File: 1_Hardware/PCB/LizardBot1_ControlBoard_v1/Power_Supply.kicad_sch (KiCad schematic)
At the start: 48 parts, among them J201 XT60-M, J202 Receptable-5.08-2P, J203 JST-PH-2-Male, J204 JST-PH-2-Male, J205 JST-PH-2-Male, J206 USB_C_Receptacle_PowerOnly_6P, Q201 SQ4425EY, SW201 SW_SPST, SW202 SW_Push, SW203 SW_SPDT, U201 MP2225, U202 AP2112K-3.3

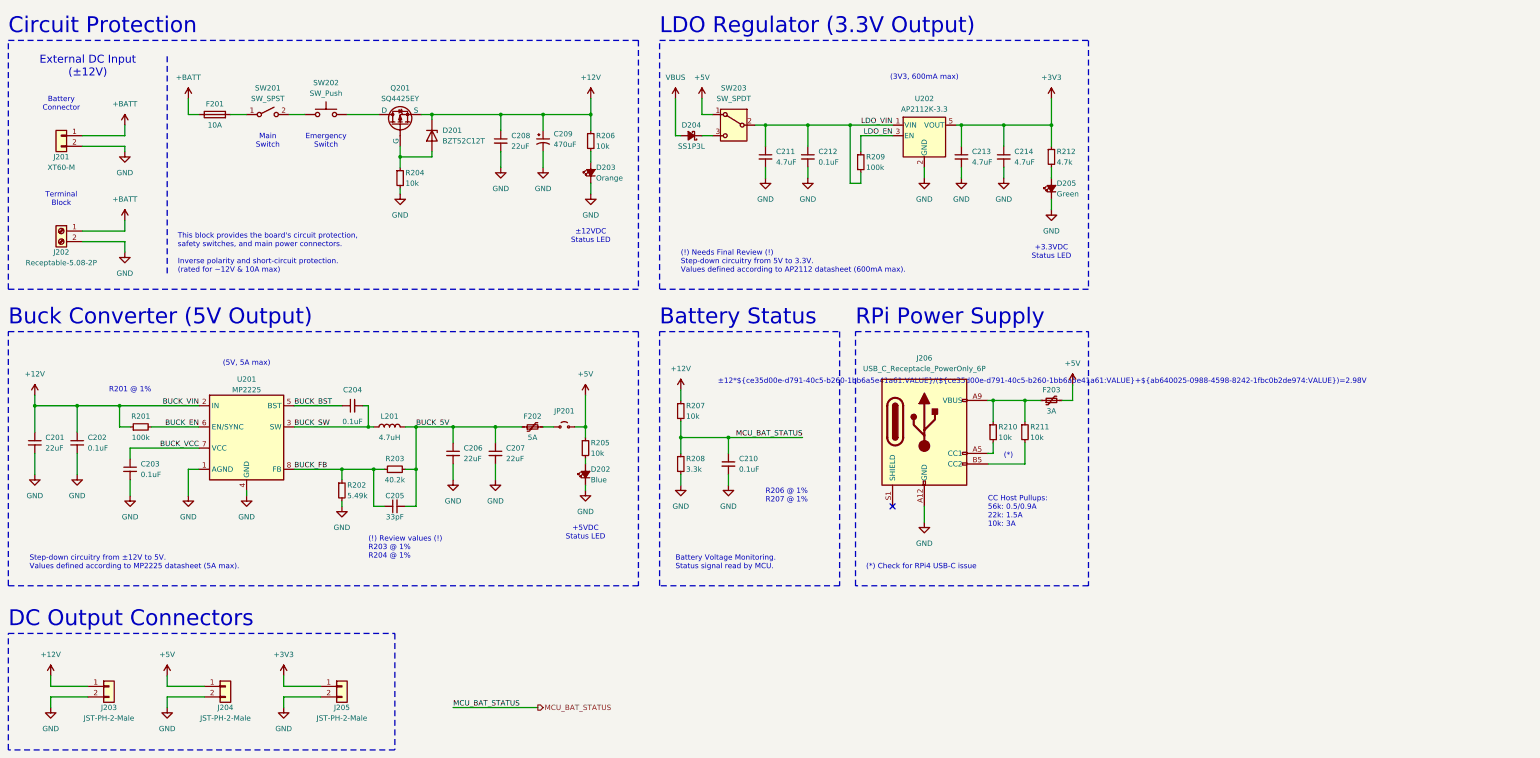
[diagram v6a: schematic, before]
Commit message: Updated schematics. Assigned footprints. Added BOM to /4_Docs.
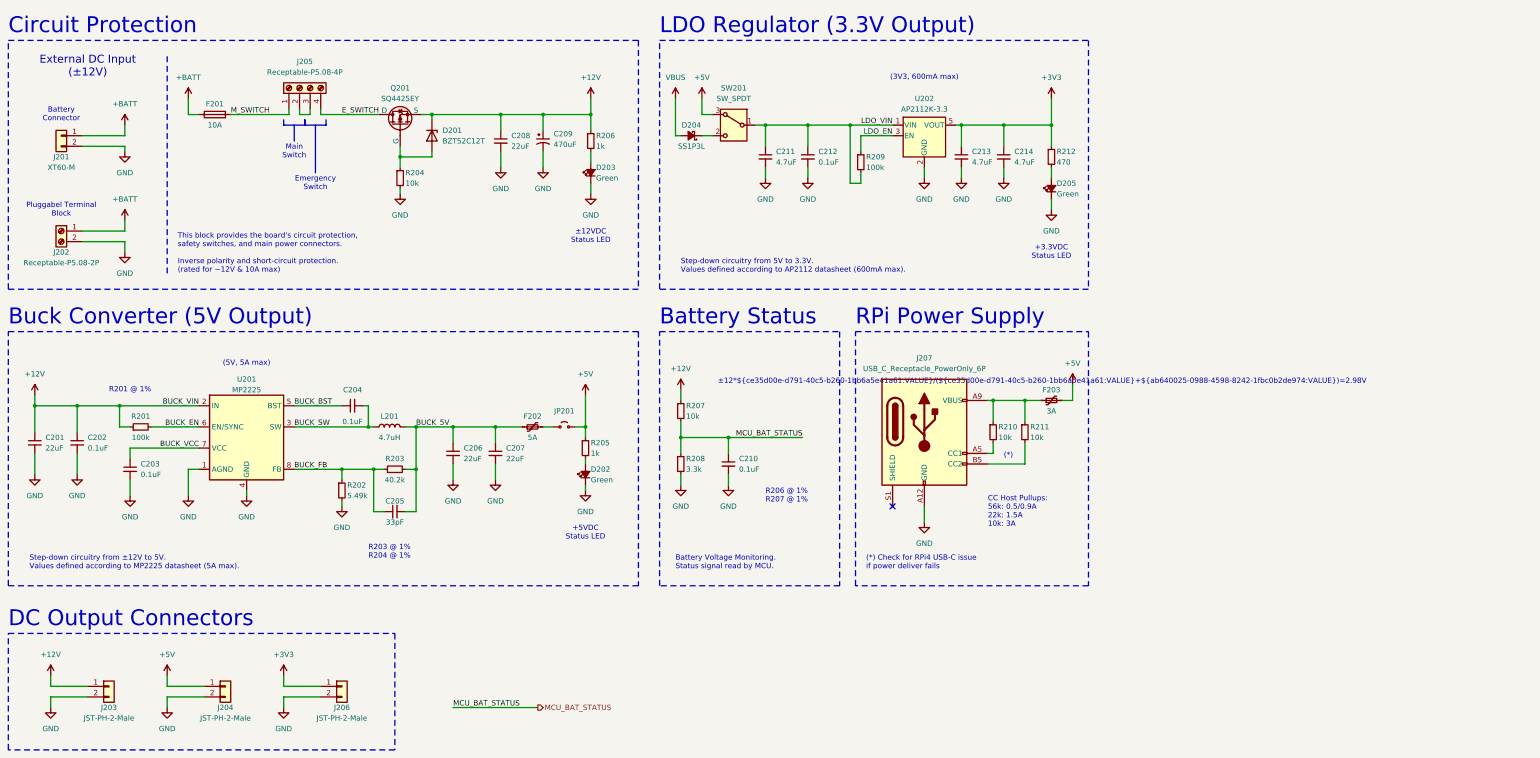
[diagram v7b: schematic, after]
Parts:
- removed SW201: SW_SPST, symbol Switch:SW_SPST
- removed SW202: SW_Push, symbol Switch:SW_Push
- removed SW203: SW_SPDT, symbol Switch:SW_SPDT
- added J205: Receptable-P5.08-4P, Connector_Phoenix_MSTB:PhoenixContact_MSTBA_2,5_4-G-5,08_1x04_P5.08mm_Horizontal, symbol Connector:Screw_Terminal_01x04
- added SW201: SW_SPDT, Button_Switch_THT:SW_Slide_SPDT_Straight_CK_OS102011MS2Q, symbol Switch:SW_SPDT_312
- C201, C202, C206, C207, C208, C211, C212, C213, C214: footprint (none) -> Capacitor_SMD:C_0805_2012Metric_Pad1.18x1.45mm_HandSolder
- C203, C204, C205, C210: footprint (none) -> Capacitor_SMD:C_0603_1608Metric_Pad1.08x0.95mm_HandSolder
- C209: footprint (none) -> Capacitor_SMD:CP_Elec_8x10
- D201: footprint (none) -> Diode_SMD:D_SOD-523
- D202: value Blue -> Green; footprint (none) -> LED_SMD:LED_0805_2012Metric_Pad1.15x1.40mm_HandSolder
- D203: value Orange -> Green; footprint (none) -> LED_SMD:LED_0805_2012Metric_Pad1.15x1.40mm_HandSolder
- D204: footprint (none) -> Diode_SMD:D_SMP_DO-220AA
- D205: footprint (none) -> LED_SMD:LED_0805_2012Metric_Pad1.15x1.40mm_HandSolder
- F201: footprint (none) -> Fuse:Fuseholder_Clip-5x20mm_Littelfuse_519_Inline_P20.60x5.00mm_D1.00mm_Horizontal
- F202: footprint (none) -> Fuse:Fuse_1812_4532Metric_Pad1.30x3.40mm_HandSolder
- F203: footprint (none) -> Fuse:Fuse_1206_3216Metric_Pad1.42x1.75mm_HandSolder
- J201: footprint (none) -> Connector_AMASS:AMASS_XT60PW-M_1x02_P7.20mm_Horizontal
- J202: value Receptable-5.08-2P -> Receptable-P5.08-2P; footprint (none) -> Connector_Phoenix_MSTB:PhoenixContact_MSTBA_2,5_2-G-5,08_1x02_P5.08mm_Horizontal
- J203, J204: footprint (none) -> Connector_JST:JST_PH_S2B-PH-K_1x02_P2.00mm_Horizontal
- J206: renamed from J205; footprint (none) -> Connector_JST:JST_PH_S2B-PH-K_1x02_P2.00mm_Horizontal
- J207: renamed from J206; footprint (none) -> Connector_USB:USB_C_Receptacle_GCT_USB4085
- JP201: footprint (none) -> Jumper:SolderJumper-2_P1.3mm_Open_TrianglePad1.0x1.5mm
- L201: footprint (none) -> Inductor_SMD:L_Bourns_SRP7028A_7.3x6.6mm
- R201, R202, R203, R204, R207, R208, R209: footprint (none) -> Resistor_SMD:R_0805_2012Metric_Pad1.20x1.40mm_HandSolder
- R205, R206: value 10k -> 1k; footprint (none) -> Resistor_SMD:R_0603_1608Metric_Pad0.98x0.95mm_HandSolder
- R210, R211: footprint (none) -> Resistor_SMD:R_0603_1608Metric_Pad0.98x0.95mm_HandSolder
- R212: value 4.7k -> 470; footprint (none) -> Resistor_SMD:R_0603_1608Metric_Pad0.98x0.95mm_HandSolder
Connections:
- net +5V: now also SW201.3 (A)
- net LDO_VIN: now also SW201.1 (B)
- net E_SWITCH: now reaches Q201.1 (D)
- net E_SWITCH: now also J205.4 (Pin_4)
- net at D204.1 (K): now also SW201.2 (C)
- net M_SWITCH: now reaches F201.2
- net M_SWITCH: now also J205.1 (Pin_1)
- new net: J205.2 (Pin_2), J205.3 (Pin_3)
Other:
- note added: "(*) Check for RPi4 USB-C issue if power deliver fails"
- note added: "Pluggabel Terminal Block"
- note added: "R203 @ 1% R204 @ 1%"
- note added: "Step-down circuitry from 5V to 3.3V. Values defined according to AP2112 datasheet (600mA max)."
- note removed: "(!) Needs Final Review (!) Step-down circuitry from 5V to 3.3V. Values defined according to AP2112 datasheet (600mA max)."
- note removed: "(!) Review values (!) R203 @ 1% R204 @ 1%"
- note removed: "(*) Check for RPi4 USB-C issue"
- note removed: "Terminal Block"
- moved on the sheet: C205

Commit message: Added PCB Stack and Design Rules. Added PCB Layout file.
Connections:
- net +12V: now also Q201.1 (S), Q201.2 (S)
- net E_SWITCH: now also Q201.5 (D), Q201.6 (D), Q201.7 (D), Q201.8 (D); no longer Q201.1 (D)
- net at D201.2 (A), R204.1: now also Q201.4 (G); no longer Q201.2 (G)
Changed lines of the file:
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@@
 		)
 		(property "Footprint" "Package_SO:SO-8_3.9x4.9mm_P1.27mm"
-			(at 110.49 38.1 0)
+			(at 130.81 43.18 0)
 			(effects
 				(font
@@
 			)
 		)
-		(property "Datasheet" "https://ngspice.sourceforge.io/docs/ngspice-html-manual/manual.xhtml#cha_MOSFETs"
+		(property "Datasheet" "https://www.vishay.com/docs/72179/sq4425ey.pdf"
+			(at 128.27 43.18 0)
+			(effects
+				(font
+					(size 1.27 1.27)
+				)
+				(hide yes)
+			)
+		)
+		(property "Description" "P-MOSFET transistor, drain/source/gate"
 			(at 125.73 43.18 0)
 			(effects
@@
 			)
 		)
-		(property "Description" "P-MOSFET transistor, drain/source/gate"
-			(at 113.03 43.18 0)
-			(effects
-				(font
-					(size 1.27 1.27)
-				)
-				(hide yes)
-			)
+		(pin "3"
 		)
-		(property "Sim.Device" "PMOS"
-			(at 130.175 43.18 0)
-			(effects
-				(font
-					(size 1.27 1.27)
-				)
-				(hide yes)
-			)
+		(pin "4"
 		)
-		(property "Sim.Type" "VDMOS"
-			(at 132.08 43.18 0)
-			(effects
-				(font
-					(size 1.27 1.27)
-				)
-				(hide yes)
-			)
-		)
-		(property "Sim.Pins" "1=D 2=G 3=S"
-			(at 128.27 43.18 0)
-			(effects
-				(font
-					(size 1.27 1.27)
-				)
-				(hide yes)
-			)
+		(pin "5"
 		)
 		(pin "1"
@@
 		(pin "2"
 		)
-		(pin "3"
+		(pin "7"
+		)
+		(pin "8"
+		)
+		(pin "6"
 		)
 		(instances
